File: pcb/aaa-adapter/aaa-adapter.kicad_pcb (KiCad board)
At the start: 2 copper layers, 57 x 46 mm, 2 parts, among them J2 AAAx3 Battery Box

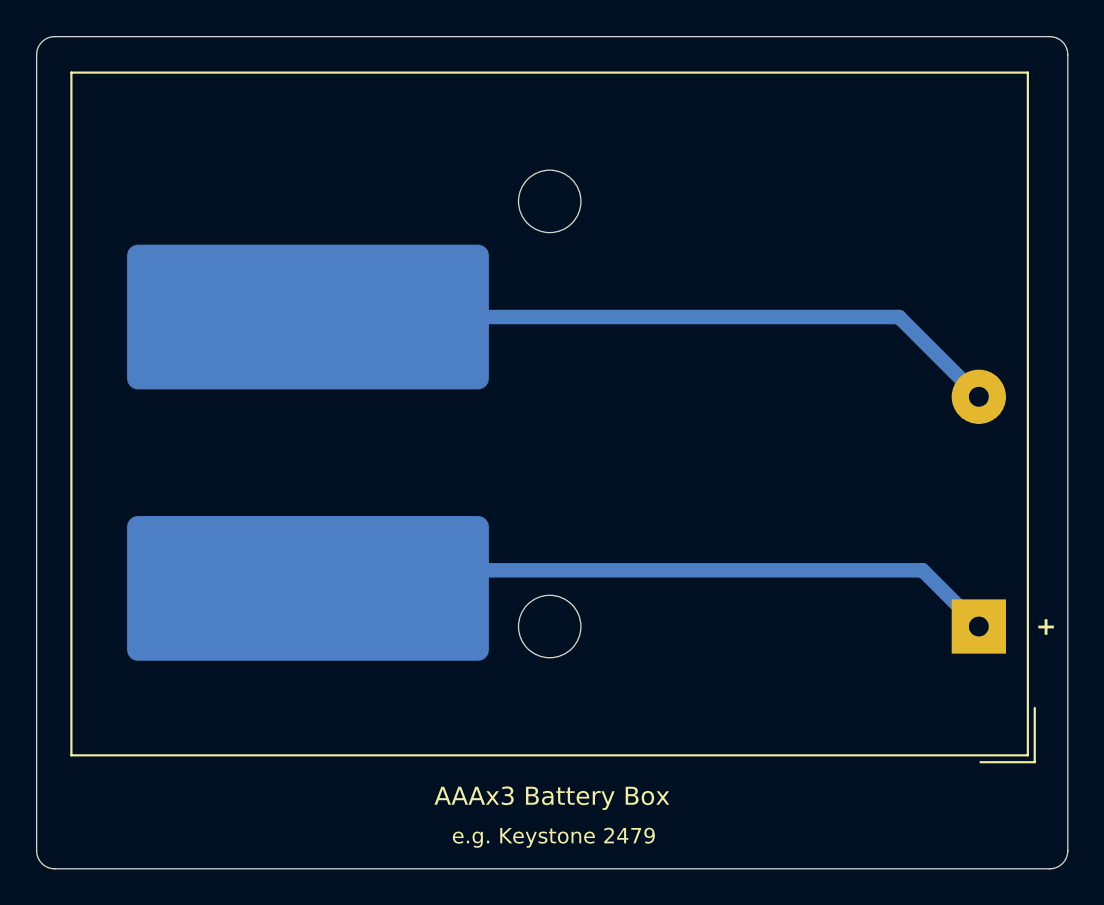
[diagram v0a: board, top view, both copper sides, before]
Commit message: Contacts weren't wide enough
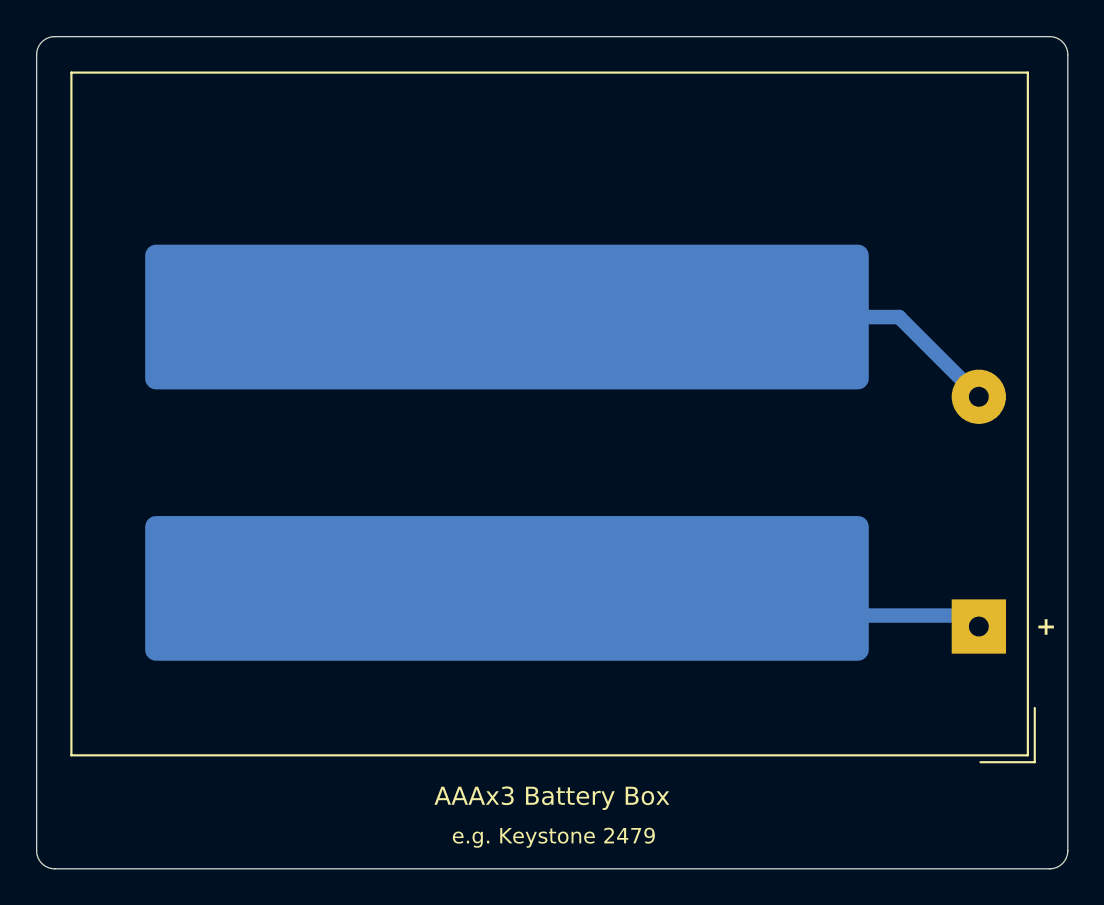
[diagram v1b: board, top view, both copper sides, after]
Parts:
- moved J1 11.0 mm to (56.0, 45.5)
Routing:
- net /V+: track 38.8 -> 27.0 mm
- net /V-: track 38.9 -> 27.9 mm
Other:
- board text added: "UP"
- board text added: "↑"
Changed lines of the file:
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@@
 			)
-		)
-		(pad "" np_thru_hole circle
-			(at 23.72 0 180)
-			(size 3.45 3.45)
-			(drill 3.45)
-			(layers "*.Cu" "*.Mask")
-		)
-		(pad "" np_thru_hole circle
-			(at 23.72 23.5 180)
-			(size 3.45 3.45)
-			(drill 3.45)
-			(layers "*.Cu" "*.Mask")
 		)
 		(pad "1" thru_hole rect
@@
 	(footprint "aaa:hp-contacts"
 		(layer "B.Cu")
-		(at 45 45.5 180)
+		(at 56 45.5 180)
 		(property "Reference" "J1"
 			(at 0 0.5 0)
@@
 		(pad "1" smd roundrect
 			(at 0 0 180)
-			(size 20 8)
+			(size 40 8)
 			(layers "B.Cu" "B.Paste" "B.Mask")
 			(roundrect_rratio 0.075)
@@
 		(pad "2" smd roundrect
 			(at 0 -15 180)
-			(size 20 8)
+			(size 40 8)
 			(layers "B.Cu" "B.Paste" "B.Mask")
 			(roundrect_rratio 0.075)
@@
 	)
 	(gr_text "+"
-		(at 33 60.5 -0)
+		(at 33.9 60.3 -0)
 		(layer "B.SilkS")
 		(effects
@@
 		)
 	)
+	(gr_text "↑"
+		(at 82.1 34.7 0)
+		(layer "B.SilkS")
+		(effects
+			(font
+				(size 4 4)
+				(thickness 0.75)
+				(bold yes)
+			)
+			(justify mirror)
+		)
+	)
+	(gr_text "UP"
+		(at 82 38.9 0)
+		(layer "B.SilkS")
+		(effects
+			(font
+				(size 1 1)
+				(thickness 0.1)
+			)
+			(justify bottom mirror)
+		)
+	)
 	(gr_text "–"
-		(at 33 45 -0)
+		(at 33.9 45.3 -0)
 		(layer "B.SilkS")
 		(effects
@@
 	)
 	(segment
-		(start 45 45.5)
+		(start 56 45.5)
 		(end 77.675001 45.5)
 		(width 0.8)
@@
 	)
 	(segment
+		(start 57.5 62)
+		(end 56 60.5)
+		(width 0.8)
+		(layer "B.Cu")
+		(net 2)
+	)
+	(segment
+		(start 81.475001 62)
+		(end 57.5 62)
+		(width 0.8)
+		(layer "B.Cu")
+		(net 2)
+	)
+	(segment
 		(start 82.082501 62.6075)
-		(end 78.975001 59.5)
-		(width 0.8)
-		(layer "B.Cu")
-		(net 2)
-	)
-	(segment
-		(start 78.975001 59.5)
-		(end 46 59.5)
-		(width 0.8)
-		(layer "B.Cu")
-		(net 2)
-	)
-	(segment
-		(start 46 59.5)
-		(end 45 60.5)
-		(width 0.8)
-		(layer "B.Cu")
+		(end 81.475001 62)
+		(width 0.8)
+		(layer "B.Cu")

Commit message: Trying flex pcb with big enough pads that it would work centered, top or bottom aligned
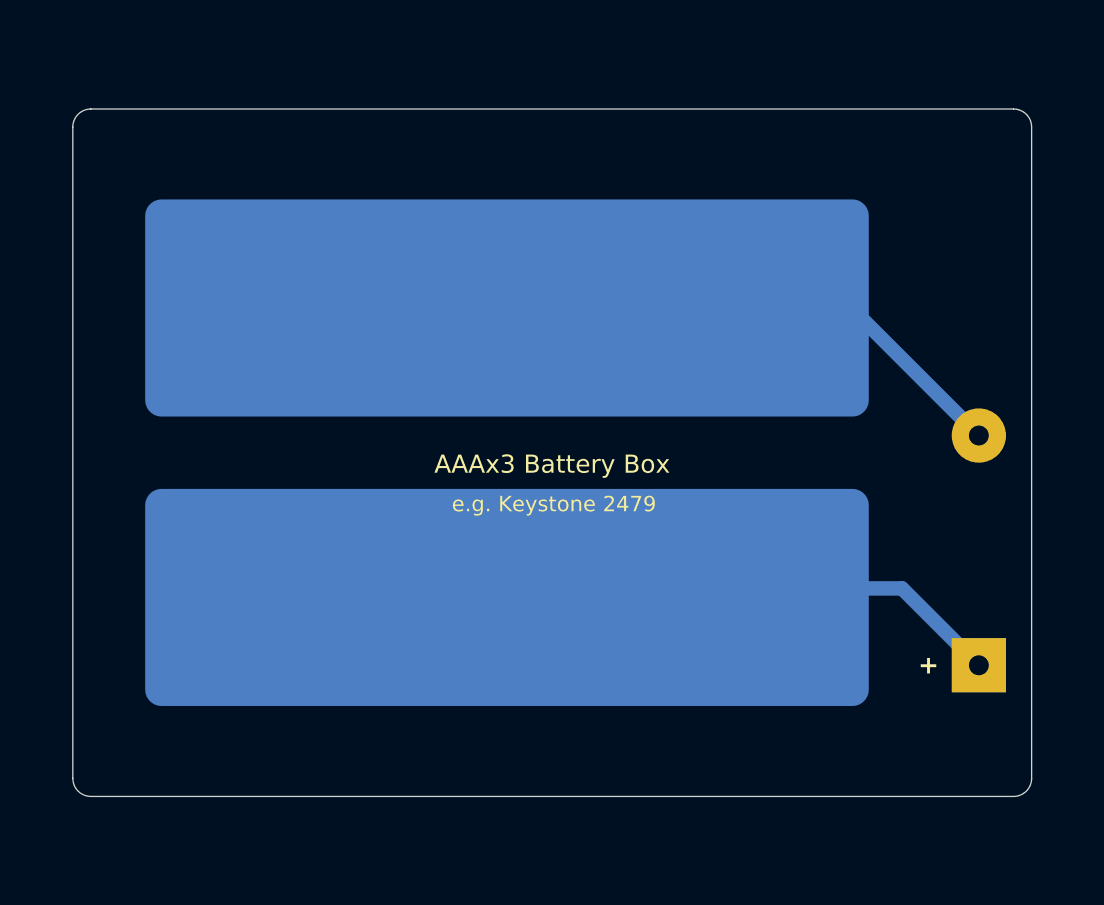
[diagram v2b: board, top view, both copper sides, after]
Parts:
- moved J2 2.14 mm to (82.1, 64.8)
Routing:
- net /V-: track 27.9 -> 28.8 mm
- net /V+: track 27.0 -> 27.8 mm
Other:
- board size 57 x 46 mm -> 53 x 38 mm
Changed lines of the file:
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@@
 	(paper "A4")
 	(title_block
-		(date "2024-08-15")
-		(rev "2")
+		(date "2024-09-05")
+		(rev "3")
 		(company "@partlyhuman")
 	)
@@
 	(footprint "Battery:BatteryHolder_Keystone_2479_3xAAA"
 		(layer "F.Cu")
-		(at 82.082501 62.6075 180)
+		(at 82.082501 64.75 180)
 		(descr "Keystone Battery Holder, 2479, Battery Type 3xAAA (Script generated with StandardBox.py) (Keystone Battery Holder, 2479, Battery Type 3xAAA)")
 		(tags "Keystone Battery Holder 2479 Battery Type 3xAAA")
@@
 		)
 		(property "Value" "AAAx3 Battery Box"
-			(at 23.582501 -9.3925 0)
+			(at 23.582501 11.1075 0)
 			(layer "F.SilkS")
 			(effects
@@
 		)
 		(property "Example Part" "e.g. Keystone 2479"
-			(at 23.482501 -11.5925 0)
+			(at 23.482501 8.9075 0)
 			(unlocked yes)
 			(layer "F.SilkS")
@@
 		(attr through_hole)
 		(fp_line
-			(start 50.16 -7.12)
-			(end 50.160001 30.62)
-			(stroke
-				(width 0.12)
-				(type solid)
-			)
-			(layer "F.SilkS")
-		)
-		(fp_line
-			(start -2.71 30.62)
-			(end 50.160001 30.62)
-			(stroke
-				(width 0.12)
-				(type solid)
-			)
-			(layer "F.SilkS")
-		)
-		(fp_line
-			(start -2.71 -7.12)
-			(end 50.16 -7.12)
-			(stroke
-				(width 0.12)
-				(type solid)
-			)
-			(layer "F.SilkS")
-		)
-		(fp_line
-			(start -2.71 -7.12)
-			(end -2.71 30.62)
-			(stroke
-				(width 0.12)
-				(type solid)
-			)
-			(layer "F.SilkS")
-		)
-		(fp_line
-			(start -3.089999 -4.5)
-			(end -3.09 -7.5)
-			(stroke
-				(width 0.12)
-				(type solid)
-			)
-			(layer "F.SilkS")
-		)
-		(fp_line
-			(start -3.09 -7.5)
-			(end -0.09 -7.499999)
-			(stroke
-				(width 0.12)
-				(type solid)
-			)
-			(layer "F.SilkS")
-		)
-		(fp_line
 			(start 50.29 -7.25)
 			(end 50.290001 30.75)
@@
 		)
 		(fp_text user "+"
-			(at -3.717499 0.0075 0)
+			(at 2.782501 0.0075 0)
 			(layer "F.SilkS")
 			(effects
@@
 		)
 		(pad "1" smd roundrect
-			(at 0 0 180)
-			(size 40 8)
+			(at 0 0.5 180)
+			(size 40 12)
 			(layers "B.Cu" "B.Paste" "B.Mask")
 			(roundrect_rratio 0.075)
@@
 		)
 		(pad "2" smd roundrect
-			(at 0 -15 180)
-			(size 40 8)
+			(at 0 -15.5 180)
+			(size 40 12)
 			(layers "B.Cu" "B.Paste" "B.Mask")
 			(roundrect_rratio 0.075)
@@
 	)
 	(gr_arc
-		(start 31 76)
-		(mid 30.292893 75.707107)
-		(end 30 75)
+		(start 85 71)
+		(mid 84.707107 71.707107)
+		(end 84 72)
+		(stroke
+			(width 0.05)
+			(type default)
+		)
+		(layer "Edge.Cuts")
+	)
+	(gr_arc
+		(start 84 34)
+		(mid 84.707107 34.292893)
+		(end 85 35)
 		(stroke
 			(width 0.05)
@@
 	)
 	(gr_line
-		(start 87 31)
-		(end 87 75)
+		(start 33 34)
+		(end 84 34)
+		(stroke
+			(width 0.05)
+			(type default)
+		)
+		(layer "Edge.Cuts")
+	)
+	(gr_line
+		(start 84 72)
+		(end 33 72)
+		(stroke
+			(width 0.05)
+			(type default)
+		)
+		(layer "Edge.Cuts")
+	)
+	(gr_line
+		(start 32 71)
+		(end 32 35)
 		(stroke
 			(width 0.05)
@@
 	)
 	(gr_arc
-		(start 30 31)
-		(mid 30.292893 30.292893)
-		(end 31 30)
+		(start 32 35)
+		(mid 32.292893 34.292893)
+		(end 33 34)
+		(stroke
+			(width 0.05)
+			(type default)
+		)
+		(layer "Edge.Cuts")
+	)
+	(gr_arc
+		(start 33 72)
+		(mid 32.292893 71.707107)
+		(end 32 71)
 		(stroke
 			(width 0.05)
@@
 	)
 	(gr_line
-		(start 30 75)
-		(end 30 31)
-		(stroke
-			(width 0.05)
-			(type default)
-		)
-		(layer "Edge.Cuts")
-	)
-	(gr_line
-		(start 86 76)
-		(end 31 76)
-		(stroke
-			(width 0.05)
-			(type default)
-		)
-		(layer "Edge.Cuts")
-	)
-	(gr_line
-		(start 31 30)
-		(end 86 30)
-		(stroke
-			(width 0.05)
-			(type default)
-		)
-		(layer "Edge.Cuts")
-	)
-	(gr_arc
-		(start 87 75)
-		(mid 86.707107 75.707107)
-		(end 86 76)
-		(stroke
-			(width 0.05)
-			(type default)
-		)
-		(layer "Edge.Cuts")
-	)
-	(gr_arc
-		(start 86 30)
-		(mid 86.707107 30.292893)
-		(end 87 31)
+		(start 85 35)
+		(end 85 71)
 		(stroke
 			(width 0.05)
@@
 		(start 30 53)
 		(end 87 53)
+		(locked yes)
 		(stroke
 			(width 0.1)
@@
 	)
 	(gr_text "Calculator battery well side"
-		(at 58.5 34.5 0)
+		(at 58.5 36.6 0)
 		(layer "B.SilkS")
 		(effects
@@
 	)
 	(gr_text "↑"
-		(at 82.1 34.7 0)
+		(at 82.1 36.8 0)
 		(layer "B.SilkS")
 		(effects
@@
 	)
 	(gr_text "UP"
-		(at 82 38.9 0)
+		(at 82 41 0)
 		(layer "B.SilkS")
 		(effects
@@
 	)
 	(segment
-		(start 56 45.5)
-		(end 77.675001 45.5)
+		(start 75.532501 45.5)
+		(end 82.082501 52.05)
 		(width 0.8)
 		(layer "B.Cu")
@@
 	)
 	(segment
-		(start 77.675001 45.5)
-		(end 82.082501 49.9075)
+		(start 56 45.5)
+		(end 75.532501 45.5)
 		(width 0.8)
 		(layer "B.Cu")
@@
 	)
 	(segment
-		(start 57.5 62)
+		(start 77.832501 60.5)
 		(end 56 60.5)
 		(width 0.8)
@@
 	)
 	(segment
-		(start 81.475001 62)
-		(end 57.5 62)
+		(start 82.082501 64.75)
+		(end 77.832501 60.5)
 		(width 0.8)
 		(layer "B.Cu")
-		(net 2)
-	)
-	(segment
-		(start 82.082501 62.6075)
-		(end 81.475001 62)
-		(width 0.8)
-		(layer "B.Cu")

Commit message: Nudge hole, frame for flex
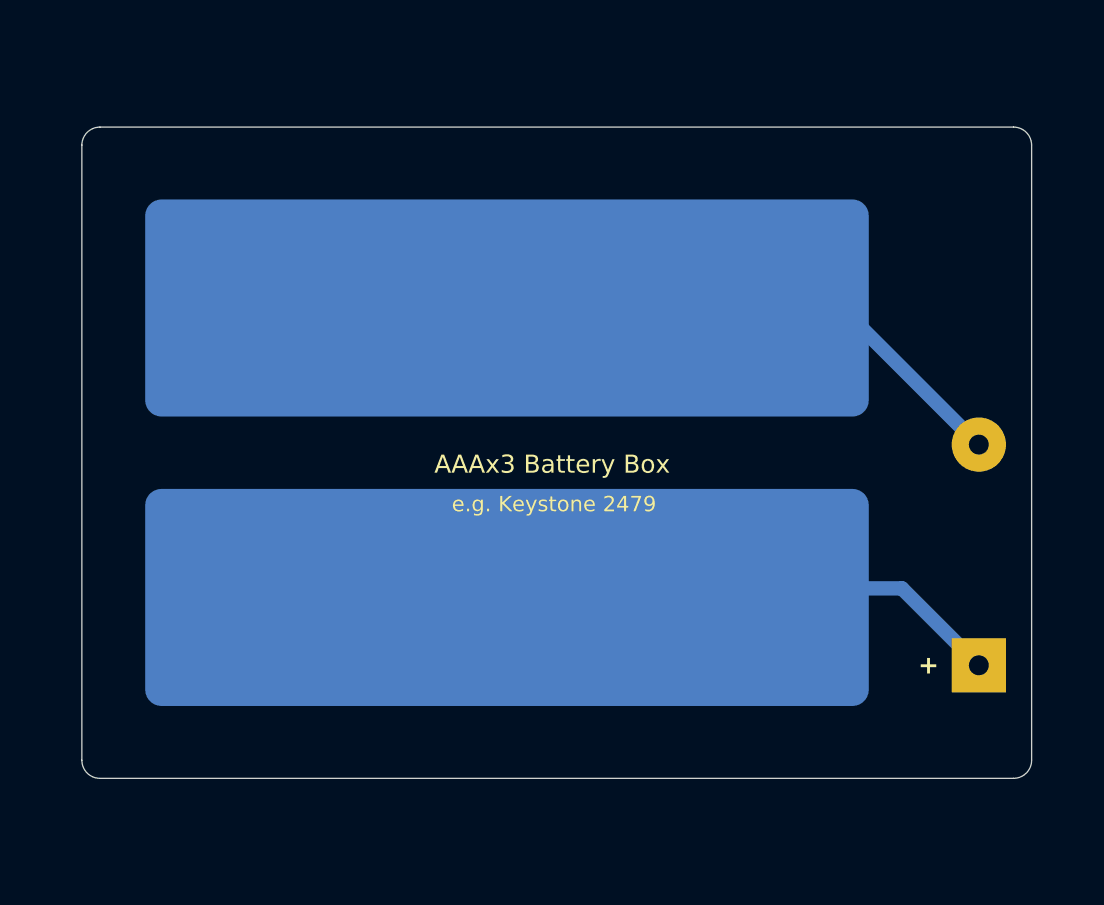
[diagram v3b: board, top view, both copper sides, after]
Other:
- board size 53 x 38 mm -> 52.5 x 36 mm
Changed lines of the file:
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@@
 		)
 		(pad "2" thru_hole circle
-			(at 0 12.7 180)
+			(at 0 12.2 180)
 			(size 3 3)
 			(drill 1.1)
@@
 	)
 	(gr_arc
-		(start 85 71)
-		(mid 84.707107 71.707107)
-		(end 84 72)
+		(start 85 70)
+		(mid 84.707107 70.707107)
+		(end 84 71)
 		(stroke
 			(width 0.05)
@@
 	)
 	(gr_arc
-		(start 84 34)
-		(mid 84.707107 34.292893)
-		(end 85 35)
-		(stroke
-			(width 0.05)
-			(type default)
-		)
-		(layer "Edge.Cuts")
-	)
-	(gr_line
-		(start 33 34)
-		(end 84 34)
-		(stroke
-			(width 0.05)
-			(type default)
-		)
-		(layer "Edge.Cuts")
-	)
-	(gr_line
-		(start 84 72)
-		(end 33 72)
-		(stroke
-			(width 0.05)
-			(type default)
-		)
-		(layer "Edge.Cuts")
-	)
-	(gr_line
-		(start 32 71)
-		(end 32 35)
+		(start 84 35)
+		(mid 84.707107 35.292893)
+		(end 85 36)
+		(stroke
+			(width 0.05)
+			(type default)
+		)
+		(layer "Edge.Cuts")
+	)
+	(gr_line
+		(start 33.5 35)
+		(end 84 35)
+		(stroke
+			(width 0.05)
+			(type default)
+		)
+		(layer "Edge.Cuts")
+	)
+	(gr_line
+		(start 84 71)
+		(end 33.5 71)
+		(stroke
+			(width 0.05)
+			(type default)
+		)
+		(layer "Edge.Cuts")
+	)
+	(gr_line
+		(start 32.5 70)
+		(end 32.5 36)
 		(stroke
 			(width 0.05)
@@
 	)
 	(gr_arc
-		(start 32 35)
-		(mid 32.292893 34.292893)
-		(end 33 34)
+		(start 32.5 36)
+		(mid 32.792893 35.292893)
+		(end 33.5 35)
 		(stroke
 			(width 0.05)
@@
 	)
 	(gr_arc
-		(start 33 72)
-		(mid 32.292893 71.707107)
-		(end 32 71)
-		(stroke
-			(width 0.05)
-			(type default)
-		)
-		(layer "Edge.Cuts")
-	)
-	(gr_line
-		(start 85 35)
-		(end 85 71)
+		(start 33.5 71)
+		(mid 32.792893 70.707107)
+		(end 32.5 70)
+		(stroke
+			(width 0.05)
+			(type default)
+		)
+		(layer "Edge.Cuts")
+	)
+	(gr_line
+		(start 85 36)
+		(end 85 70)
 		(stroke
 			(width 0.05)
@@
 	)
 	(gr_text "Calculator battery well side"
-		(at 58.5 36.6 0)
+		(at 58.5 37.5 0)
 		(layer "B.SilkS")
 		(effects
@@
 	)
 	(gr_text "↑"
-		(at 82.1 36.8 0)
+		(at 82.1 37.5 0)
 		(layer "B.SilkS")
 		(effects
@@
 	)
 	(gr_text "UP"
-		(at 82 41 0)
+		(at 82 41.7 0)
 		(layer "B.SilkS")
 		(effects
@@
 	)
 	(segment
-		(start 75.532501 45.5)
-		(end 82.082501 52.05)
+		(start 75 45.5)
+		(end 82.05 52.55)
 		(width 0.8)
 		(layer "B.Cu")
@@
 	(segment
 		(start 56 45.5)
-		(end 75.532501 45.5)
+		(end 75 45.5)
 		(width 0.8)
 		(layer "B.Cu")
+		(net 1)
+	)
+	(segment
+		(start 82.05 52.55)
+		(end 82.082501 52.55)
+		(width 0.8)
+		(layer "B.Cu")
